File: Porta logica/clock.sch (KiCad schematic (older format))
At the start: 15 parts, among them P4 Ext_Clock, U6 74HC00, U7 LM555N

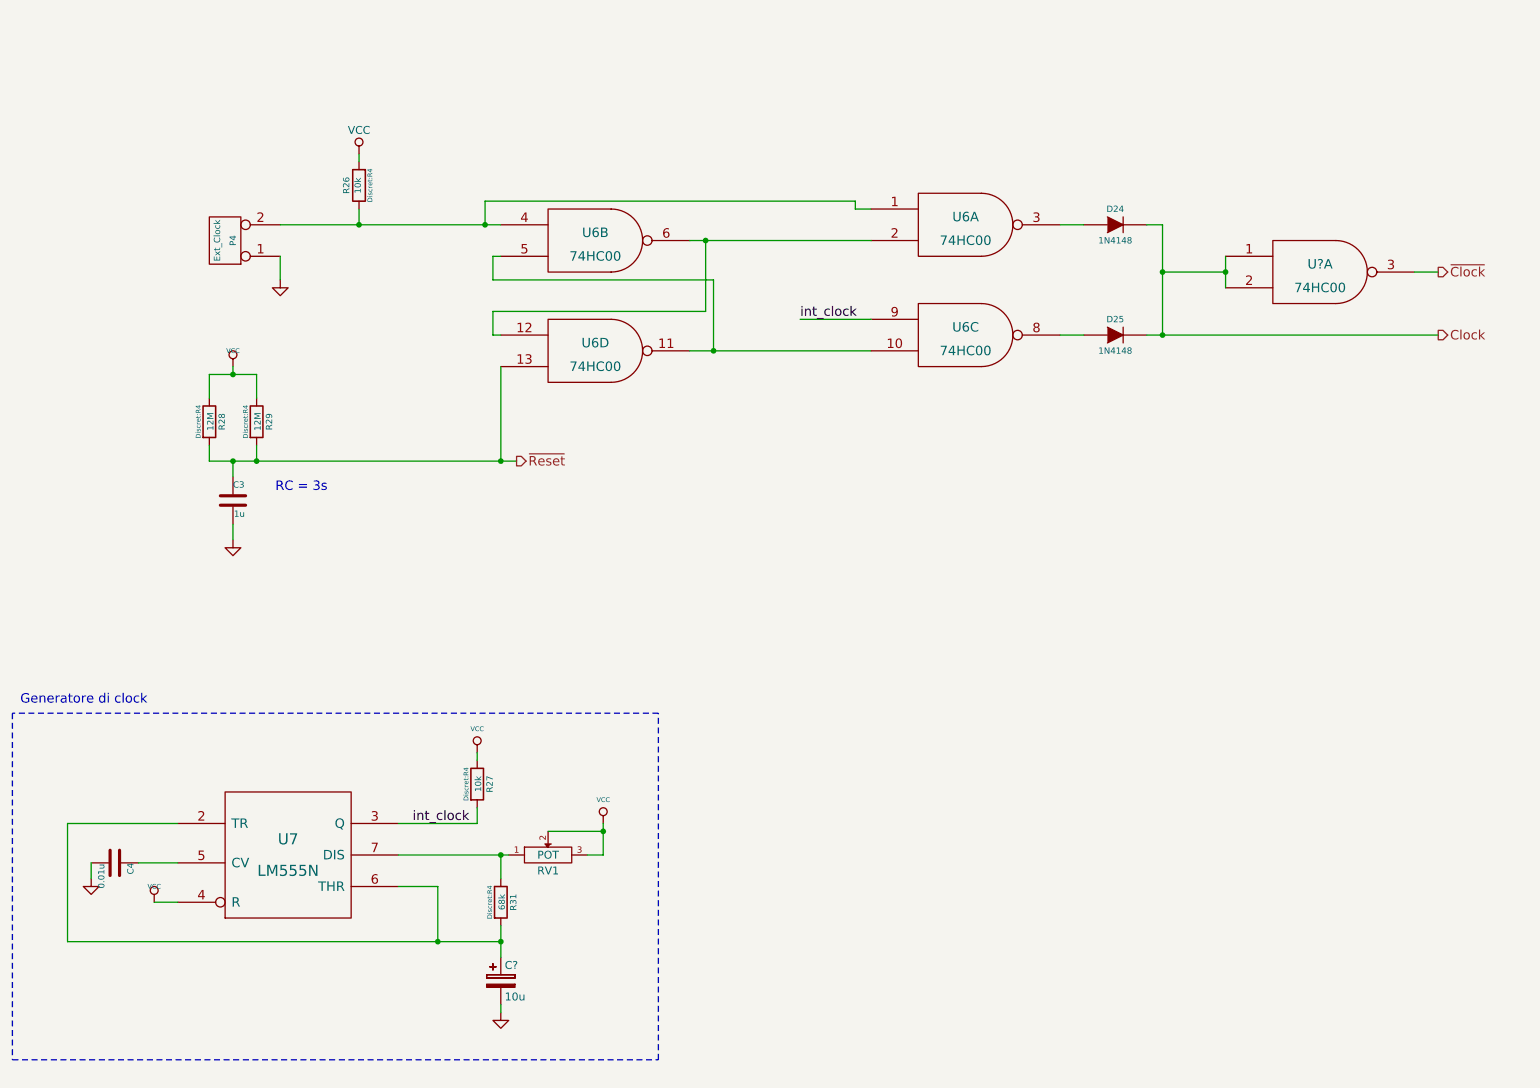
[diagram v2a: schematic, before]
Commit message: Completata annotazione e associazione di footprint
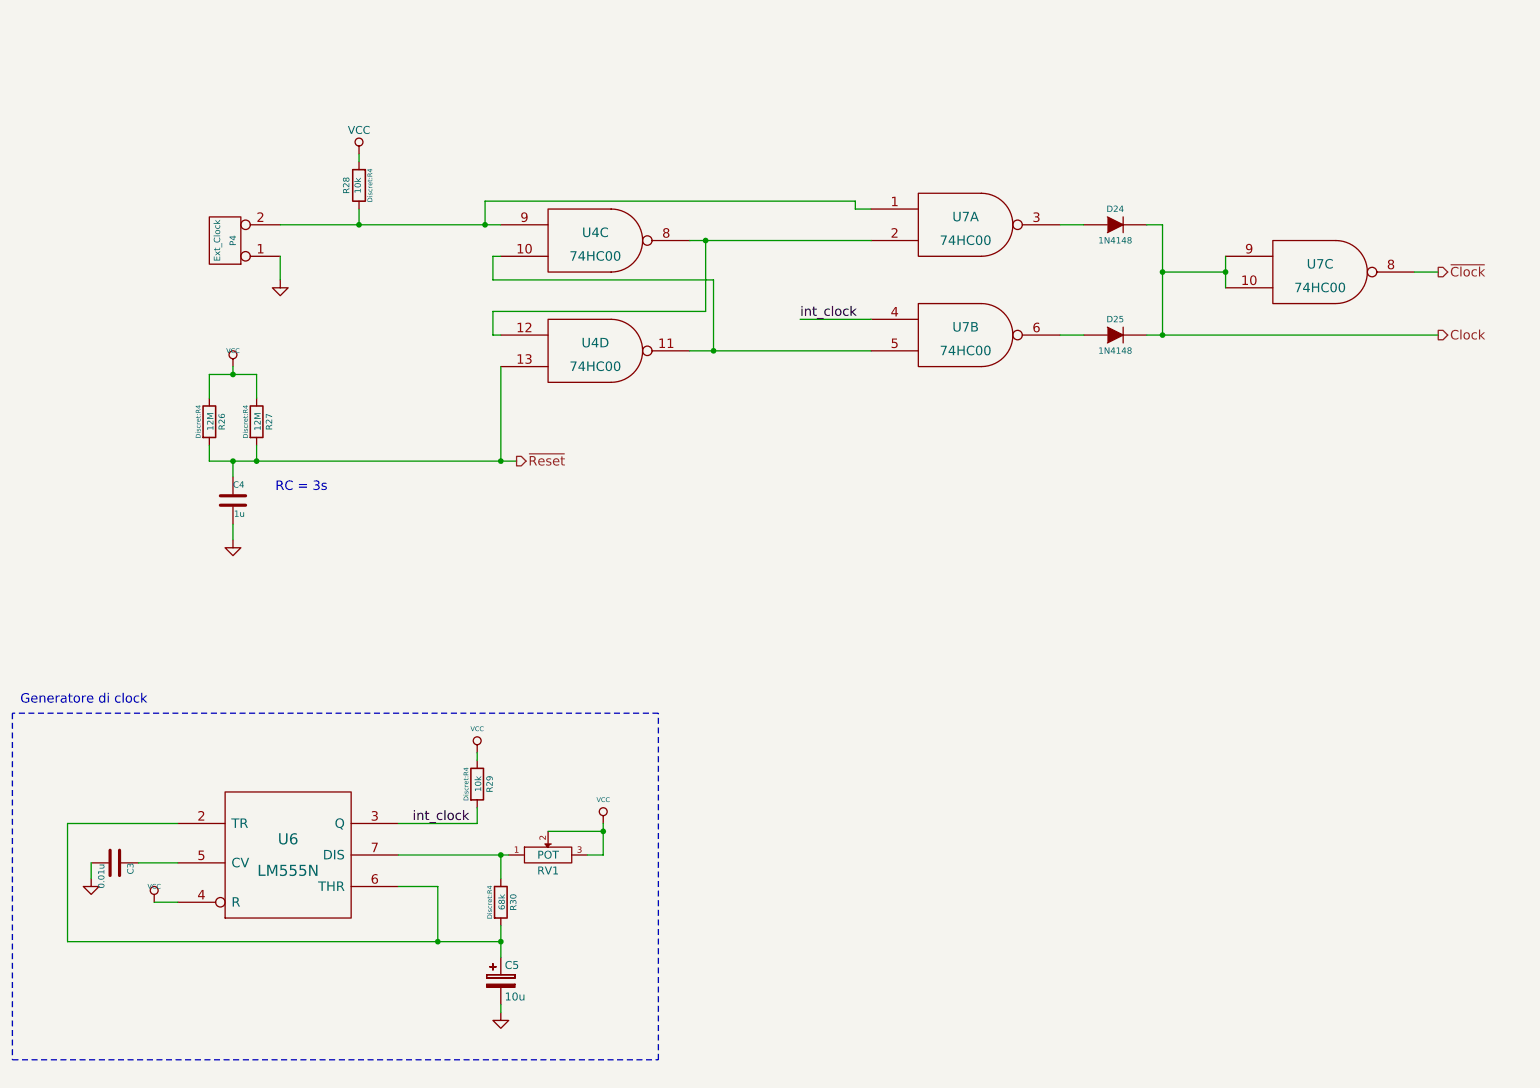
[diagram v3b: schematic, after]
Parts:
- C5: renamed from C?; footprint (none) -> Capacitors_Elko_ThroughHole:Elko_vert_11.2x6.3mm_RM2.5
- U4: renamed from U6; footprint Housings_SSOP:SSOP-14_5.3x6.2mm_Pitch0.65mm -> Housings_SOIC:SOIC-16_7.5x10.3mm_Pitch1.27mm
- U6: renamed from U7; footprint Housings_SOIC:SOIC-8_3.9x4.9mm_Pitch1.27mm -> Housings_SSOP:SSOP-14_5.3x6.2mm_Pitch0.65mm
- U7: renamed from U6; footprint Housings_SSOP:SSOP-14_5.3x6.2mm_Pitch0.65mm -> Housings_SOIC:SOIC-8_3.9x4.9mm_Pitch1.27mm
- U7: renamed from U?; footprint Housings_SOIC:SOIC-14_3.9x8.7mm_Pitch1.27mm -> Housings_SOIC:SOIC-8_3.9x4.9mm_Pitch1.27mm
- renumbered C4 to C3, C3 to C4, R28 to R26, R29 to R27, R26 to R28, R27 to R29, R31 to R30
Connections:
- net Clock: now also U7.10, U7.9; no longer U7.1, U7.2
- net int_clock: now also U7.4; no longer U7.9
- net ~Clock: now also U7.8; no longer U7.3
- net at P4.2 (PM), R28.1, U7.1: now also U4.9; no longer U4.4
- net at U4.12, U7.2: now also U4.8; no longer U4.6
- net at D25.1 (A): now also U7.6; no longer U7.8
- new net: U4.10, U4.11, U7.5
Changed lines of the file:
@@
 $EndDescr
 $Comp
-L LM555N U7
+L LM555N U6
 U 1 1 555C383B
 P 3050 5850
-F 0 "U7" H 3050 5950 70  0000 C CNN
+F 0 "U6" H 3050 5950 70  0000 C CNN
 F 1 "LM555N" H 3050 5750 70  0000 C CNN
-F 2 "Housings_SOIC:SOIC-8_3.9x4.9mm_Pitch1.27mm" H 3050 5850 60  0001 C CNN
+F 2 "Housings_SSOP:SSOP-14_5.3x6.2mm_Pitch0.65mm" H 3050 5850 60  0001 C CNN
 F 3 "" H 3050 5850 60  0000 C CNN
 	1    3050 5850
@@
 $EndComp
 $Comp
-L VCC #PWR016
+L VCC #PWR17
 U 1 1 555C3841
 P 2200 6150
-F 0 "#PWR016" H 2200 6250 30  0001 C CNN
+F 0 "#PWR17" H 2200 6250 30  0001 C CNN
 F 1 "VCC" H 2200 6250 30  0000 C CNN
 F 2 "" H 2200 6150 60  0000 C CNN
@@
 $EndComp
 $Comp
-L C C4
+L C C3
 U 1 1 555C3847
 P 1950 5900
-AR Path="/555C3847" Ref="C4"  Part="1"
-AR Path="/555C3620/555C3847" Ref="C4"  Part="1"
-F 0 "C4" H 1950 6000 40  0000 L CNN
+F 0 "C3" H 1950 6000 40  0000 L CNN
 F 1 "0.01u" H 1956 5815 40  0000 L CNN
 F 2 "Capacitors_Elko_ThroughHole:Elko_vert_11.2x6.3mm_RM2.5" H 1988 5750 30  0001 C CNN
@@
 $EndComp
 $Comp
-L GND #PWR020
+L GND #PWR16
 U 1 1 555C384D
 P 1800 6000
-AR Path="/555C384D" Ref="#PWR020"  Part="1"
-AR Path="/555C3620/555C384D" Ref="#PWR017"  Part="1"
-F 0 "#PWR017" H 1800 6000 30  0001 C CNN
+F 0 "#PWR16" H 1800 6000 30  0001 C CNN
 F 1 "GND" H 1800 5930 30  0001 C CNN
 F 2 "" H 1800 6000 60  0000 C CNN
@@
 $EndComp
 $Comp
-L R R31
+L R R30
 U 1 1 555C3853
 P 4400 6150
-AR Path="/555C3853" Ref="R31"  Part="1"
-AR Path="/555C3620/555C3853" Ref="R31"  Part="1"
-F 0 "R31" V 4480 6150 40  0000 C CNN
+F 0 "R30" V 4480 6150 40  0000 C CNN
 F 1 "68k" V 4407 6151 40  0000 C CNN
 F 2 "Discret:R4" V 4330 6150 30  0000 C CNN
@@
 $EndComp
 $Comp
-L VCC #PWR018
+L VCC #PWR24
 U 1 1 555C3865
 P 5050 5650
-F 0 "#PWR018" H 5050 5750 30  0001 C CNN
+F 0 "#PWR24" H 5050 5750 30  0001 C CNN
 F 1 "VCC" H 5050 5800 30  0000 C CNN
 F 2 "" H 5050 5650 60  0000 C CNN
@@
 $EndComp
 $Comp
-L GND #PWR022
+L GND #PWR23
 U 1 1 555C386B
 P 4400 6850
-AR Path="/555C386B" Ref="#PWR022"  Part="1"
-AR Path="/555C3620/555C386B" Ref="#PWR019"  Part="1"
-F 0 "#PWR019" H 4400 6850 30  0001 C CNN
+F 0 "#PWR23" H 4400 6850 30  0001 C CNN
 F 1 "GND" H 4400 6780 30  0001 C CNN
 F 2 "" H 4400 6850 60  0000 C CNN
@@
 $EndComp
 $Comp
-L GND #PWR023
+L GND #PWR20
 U 1 1 555C5E35
 P 3000 2200
-AR Path="/555C5E35" Ref="#PWR023"  Part="1"
-AR Path="/555C3620/555C5E35" Ref="#PWR020"  Part="1"
-F 0 "#PWR020" H 3000 2200 30  0001 C CNN
+F 0 "#PWR20" H 3000 2200 30  0001 C CNN
 F 1 "GND" H 3000 2130 30  0001 C CNN
 F 2 "" H 3000 2200 60  0000 C CNN
@@
 $EndComp
 $Comp
-L 74HC00 U6
-U 2 1 555C5E57
+L 74HC00 U4
+U 3 1 555C5E57
 P 5000 1950
-F 0 "U6" H 5000 2000 60  0000 C CNN
+F 0 "U4" H 5000 2000 60  0000 C CNN
 F 1 "74HC00" H 5000 1850 60  0000 C CNN
-F 2 "Housings_SSOP:SSOP-14_5.3x6.2mm_Pitch0.65mm" H 5000 1950 60  0001 C CNN
+F 2 "Housings_SOIC:SOIC-16_7.5x10.3mm_Pitch1.27mm" H 5000 1950 60  0001 C CNN
 F 3 "~" H 5000 1950 60  0000 C CNN
-	2    5000 1950
-	1    0    0    -1
-$EndComp
-$Comp
-L 74HC00 U6
+	3    5000 1950
+	1    0    0    -1
+$EndComp
+$Comp
+L 74HC00 U4
 U 4 1 555C5E69
 P 5000 2650
-F 0 "U6" H 5000 2700 60  0000 C CNN
+F 0 "U4" H 5000 2700 60  0000 C CNN
 F 1 "74HC00" H 5000 2550 60  0000 C CNN
-F 2 "Housings_SSOP:SSOP-14_5.3x6.2mm_Pitch0.65mm" H 5000 2650 60  0001 C CNN
+F 2 "Housings_SOIC:SOIC-16_7.5x10.3mm_Pitch1.27mm" H 5000 2650 60  0001 C CNN
 F 3 "~" H 5000 2650 60  0000 C CNN
 	4    5000 2650
@@
 $EndComp
 $Comp
-L 74HC00 U6
+L 74HC00 U7
 U 1 1 555C5E6F
 P 7350 1850
-F 0 "U6" H 7350 1900 60  0000 C CNN
+F 0 "U7" H 7350 1900 60  0000 C CNN
 F 1 "74HC00" H 7350 1750 60  0000 C CNN
-F 2 "Housings_SSOP:SSOP-14_5.3x6.2mm_Pitch0.65mm" H 7350 1850 60  0001 C CNN
+F 2 "Housings_SOIC:SOIC-8_3.9x4.9mm_Pitch1.27mm" H 7350 1850 60  0001 C CNN
 F 3 "~" H 7350 1850 60  0000 C CNN
 	1    7350 1850
@@
 $EndComp
 $Comp
-L 74HC00 U6
-U 3 1 555C5E75
+L 74HC00 U7
+U 2 1 555C5E75
 P 7350 2550
-F 0 "U6" H 7350 2600 60  0000 C CNN
+F 0 "U7" H 7350 2600 60  0000 C CNN
 F 1 "74HC00" H 7350 2450 60  0000 C CNN
-F 2 "Housings_SSOP:SSOP-14_5.3x6.2mm_Pitch0.65mm" H 7350 2550 60  0001 C CNN
+F 2 "Housings_SOIC:SOIC-8_3.9x4.9mm_Pitch1.27mm" H 7350 2550 60  0001 C CNN
 F 3 "~" H 7350 2550 60  0000 C CNN
-	3    7350 2550
-	1    0    0    -1
-$EndComp
-$Comp
-L VCC #PWR021
+	2    7350 2550
+	1    0    0    -1
+$EndComp
+$Comp
+L VCC #PWR18
 U 1 1 555C5F80
 P 2700 2750
-F 0 "#PWR021" H 2700 2850 30  0001 C CNN
+F 0 "#PWR18" H 2700 2850 30  0001 C CNN
 F 1 "VCC" H 2700 2850 30  0000 C CNN
 F 2 "" H 2700 2750 60  0000 C CNN
@@
 $EndComp
 $Comp
-L GND #PWR025
+L GND #PWR19
 U 1 1 555C5F8F
 P 2700 3850
-AR Path="/555C5F8F" Ref="#PWR025"  Part="1"
-AR Path="/555C3620/555C5F8F" Ref="#PWR022"  Part="1"
-F 0 "#PWR022" H 2700 3850 30  0001 C CNN
+F 0 "#PWR19" H 2700 3850 30  0001 C CNN
 F 1 "GND" H 2700 3780 30  0001 C CNN
 F 2 "" H 2700 3850 60  0000 C CNN
@@
 $EndComp
 $Comp
-L C C3
+L C C4
 U 1 1 555C5F9E
 P 2700 3600
-AR Path="/555C5F9E" Ref="C3"  Part="1"
-AR Path="/555C3620/555C5F9E" Ref="C3"  Part="1"
-F 0 "C3" H 2700 3700 40  0000 L CNN
+F 0 "C4" H 2700 3700 40  0000 L CNN
 F 1 "1u" H 2706 3515 40  0000 L CNN
 F 2 "Capacitors_Elko_ThroughHole:Elko_vert_11.2x6.3mm_RM2.5" H 2738 3450 30  0001 C CNN
@@
 $EndComp
 $Comp
-L R R29
+L R R27
 U 1 1 555C7D7C
 P 2850 3100
-AR Path="/555C7D7C" Ref="R29"  Part="1"
-AR Path="/555C3620/555C7D7C" Ref="R29"  Part="1"
-F 0 "R29" V 2930 3100 40  0000 C CNN
+F 0 "R27" V 2930 3100 40  0000 C CNN
 F 1 "12M" V 2857 3101 40  0000 C CNN
 F 2 "Discret:R4" V 2780 3100 30  0000 C CNN
@@
 $EndComp
 $Comp
-L R R28
+L R R26
 U 1 1 555C7D82
 P 2550 3100
-AR Path="/555C7D82" Ref="R28"  Part="1"
-AR Path="/555C3620/555C7D82" Ref="R28"  Part="1"
-F 0 "R28" V 2630 3100 40  0000 C CNN
+F 0 "R26" V 2630 3100 40  0000 C CNN
 F 1 "12M" V 2557 3101 40  0000 C CNN
 F 2 "Discret:R4" V 2480 3100 30  0000 C CNN
@@
 RC = 3s
 $Comp
-L R R27
+L R R29
 U 1 1 555CE354
 P 4250 5400
-AR Path="/555CE354" Ref="R27"  Part="1"
-AR Path="/555C3620/555CE354" Ref="R27"  Part="1"
-F 0 "R27" V 4330 5400 40  0000 C CNN
+F 0 "R29" V 4330 5400 40  0000 C CNN
 F 1 "10k" V 4257 5401 40  0000 C CNN
 F 2 "Discret:R4" V 4180 5400 30  0000 C CNN
@@
 $EndComp
 $Comp
-L VCC #PWR023
+L VCC #PWR22
 U 1 1 555CE368
 P 4250 5200
-F 0 "#PWR023" H 4250 5300 30  0001 C CNN
+F 0 "#PWR22" H 4250 5300 30  0001 C CNN
 F 1 "VCC" H 4250 5350 30  0000 C CNN
 F 2 "" H 4250 5200 60  0000 C CNN
@@
 $EndComp
 $Comp
-L R R26
+L R R28
 U 1 1 555CE3C6
 P 3500 1600
-AR Path="/555CE3C6" Ref="R26"  Part="1"
-AR Path="/555C3620/555CE3C6" Ref="R26"  Part="1"
-F 0 "R26" V 3580 1600 40  0000 C CNN
+F 0 "R28" V 3580 1600 40  0000 C CNN
 F 1 "10k" V 3507 1601 40  0000 C CNN
 F 2 "Discret:R4" V 3430 1600 30  0000 C CNN
@@
 $EndComp
 $Comp
-L VCC #PWR?
+L VCC #PWR21
 U 1 1 555E3B84
 P 3500 1400
-F 0 "#PWR?" H 3500 1250 50  0001 C CNN
+F 0 "#PWR21" H 3500 1250 50  0001 C CNN
 F 1 "VCC" H 3500 1550 50  0000 C CNN
 F 2 "" H 3500 1400 60  0000 C CNN
@@
 $EndComp
 $Comp
-L CP C?
+L CP C5
 U 1 1 555EF972
 P 4400 6650
-F 0 "C?" H 4425 6750 50  0000 L CNN
+F 0 "C5" H 4425 6750 50  0000 L CNN
 F 1 "10u" H 4425 6550 50  0000 L CNN
-F 2 "" H 4438 6500 30  0000 C CNN
+F 2 "Capacitors_Elko_ThroughHole:Elko_vert_11.2x6.3mm_RM2.5" H 4438 6500 30  0001 C CNN
 F 3 "" H 4400 6650 60  0000 C CNN
 	1    4400 6650
@@
 Generatore di clock
 $Comp
-L 74HC00 U?
-U 1 1 555F65B1
+L 74HC00 U7
+U 3 1 555F65B1
 P 9600 2150
-F 0 "U?" H 9600 2200 60  0000 C CNN
+F 0 "U7" H 9600 2200 60  0000 C CNN
 F 1 "74HC00" H 9600 2050 60  0000 C CNN
-F 2 "Housings_SOIC:SOIC-14_3.9x8.7mm_Pitch1.27mm" H 9600 2150 60  0001 C CNN
+F 2 "Housings_SOIC:SOIC-8_3.9x4.9mm_Pitch1.27mm" H 9600 2150 60  0001 C CNN
 F 3 "~" H 9600 2150 60  0000 C CNN
-	1    9600 2150
-	1    0    0    -1
-$EndComp
+	3    9600 2150
+	1    0    0    -1
+$EndComp

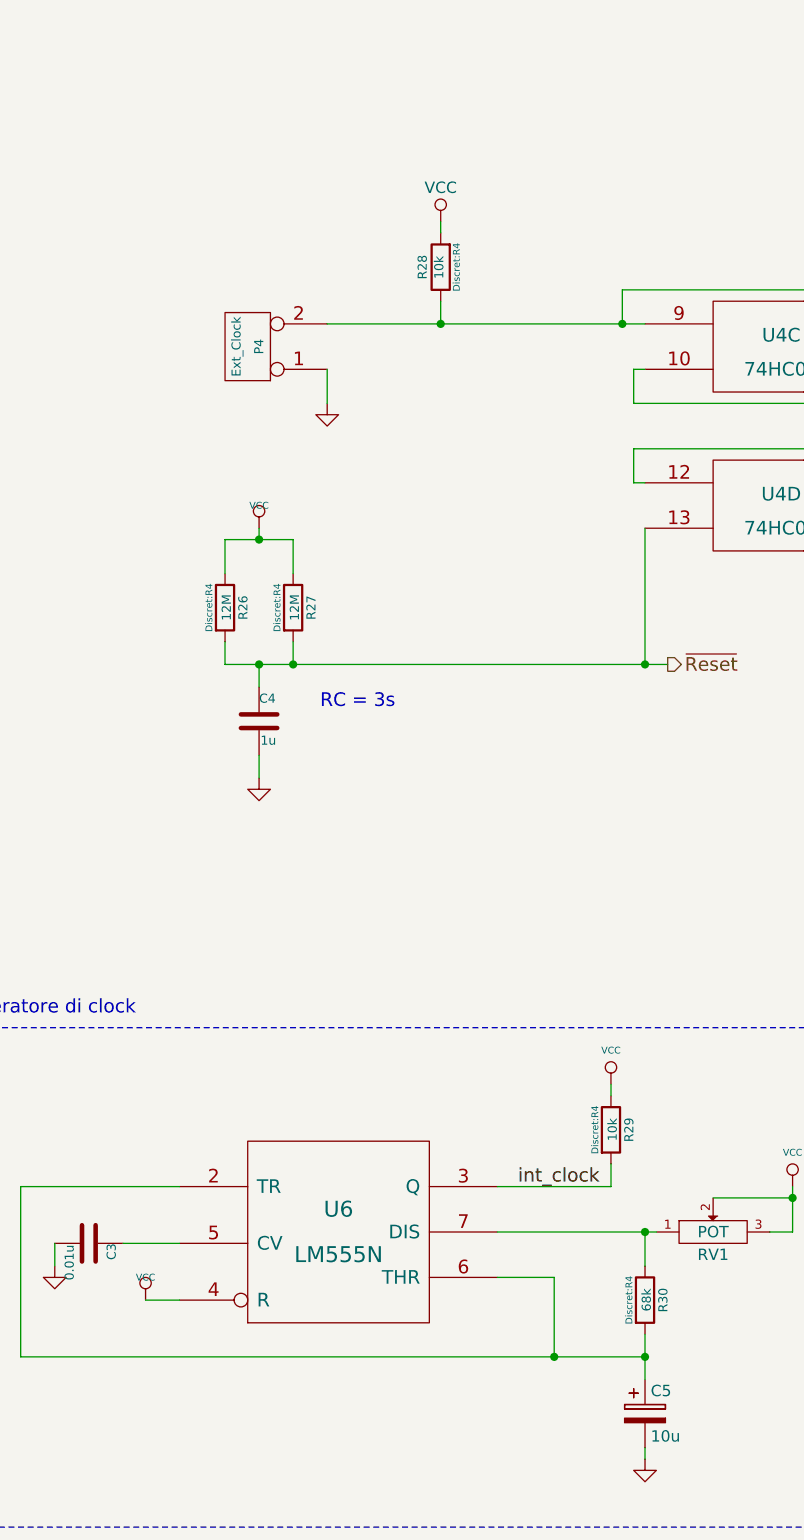
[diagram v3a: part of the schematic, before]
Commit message: Aggiorna footprint resistenze
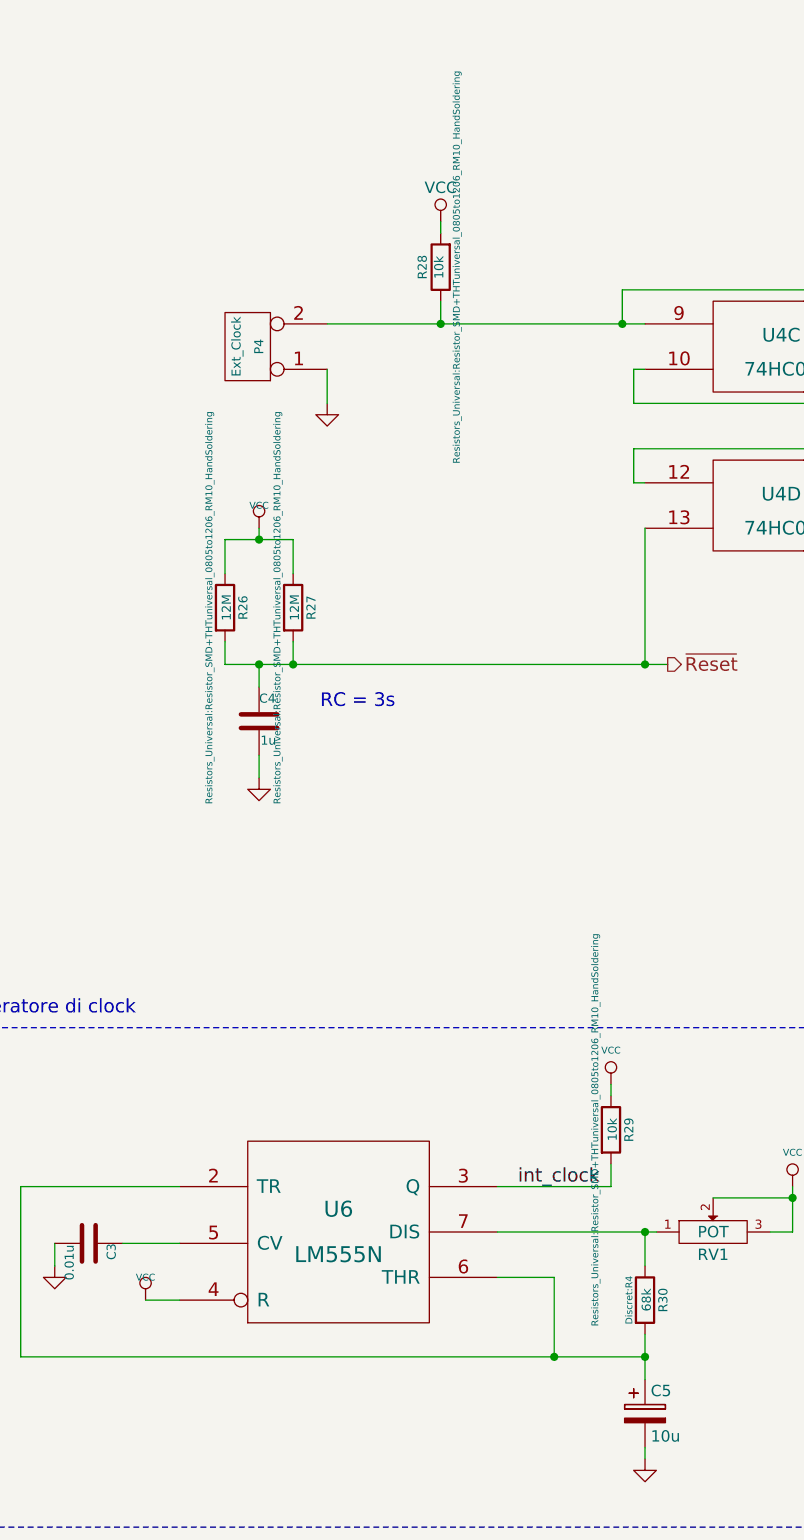
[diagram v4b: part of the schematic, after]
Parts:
- R26, R27, R28, R29: footprint Discret:R4 -> Resistors_Universal:Resistor_SMD+THTuniversal_0805to1206_RM10_HandSoldering
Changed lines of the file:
@@
 F 0 "R27" V 2930 3100 40  0000 C CNN
 F 1 "12M" V 2857 3101 40  0000 C CNN
-F 2 "Discret:R4" V 2780 3100 30  0000 C CNN
+F 2 "Resistors_Universal:Resistor_SMD+THTuniversal_0805to1206_RM10_HandSoldering" V 2780 3100 30  0000 C CNN
 F 3 "~" H 2850 3100 30  0000 C CNN
 	1    2850 3100
@@
 F 0 "R26" V 2630 3100 40  0000 C CNN
 F 1 "12M" V 2557 3101 40  0000 C CNN
-F 2 "Discret:R4" V 2480 3100 30  0000 C CNN
+F 2 "Resistors_Universal:Resistor_SMD+THTuniversal_0805to1206_RM10_HandSoldering" V 2480 3100 30  0000 C CNN
 F 3 "~" H 2550 3100 30  0000 C CNN
 	1    2550 3100
@@
 F 0 "R29" V 4330 5400 40  0000 C CNN
 F 1 "10k" V 4257 5401 40  0000 C CNN
-F 2 "Discret:R4" V 4180 5400 30  0000 C CNN
+F 2 "Resistors_Universal:Resistor_SMD+THTuniversal_0805to1206_RM10_HandSoldering" V 4180 5400 30  0000 C CNN
 F 3 "~" H 4250 5400 30  0000 C CNN
 	1    4250 5400
@@
 F 0 "R28" V 3580 1600 40  0000 C CNN
 F 1 "10k" V 3507 1601 40  0000 C CNN
-F 2 "Discret:R4" V 3430 1600 30  0000 C CNN
+F 2 "Resistors_Universal:Resistor_SMD+THTuniversal_0805to1206_RM10_HandSoldering" V 3430 1600 30  0000 C CNN
 F 3 "~" H 3500 1600 30  0000 C CNN
 	1    3500 1600
